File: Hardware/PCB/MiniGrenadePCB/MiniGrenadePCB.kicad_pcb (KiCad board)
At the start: 2 copper layers, 44.5 x 52.1 mm, 3 parts, among them U1 DF-Player_mini, U2 WeMos_D1_mini

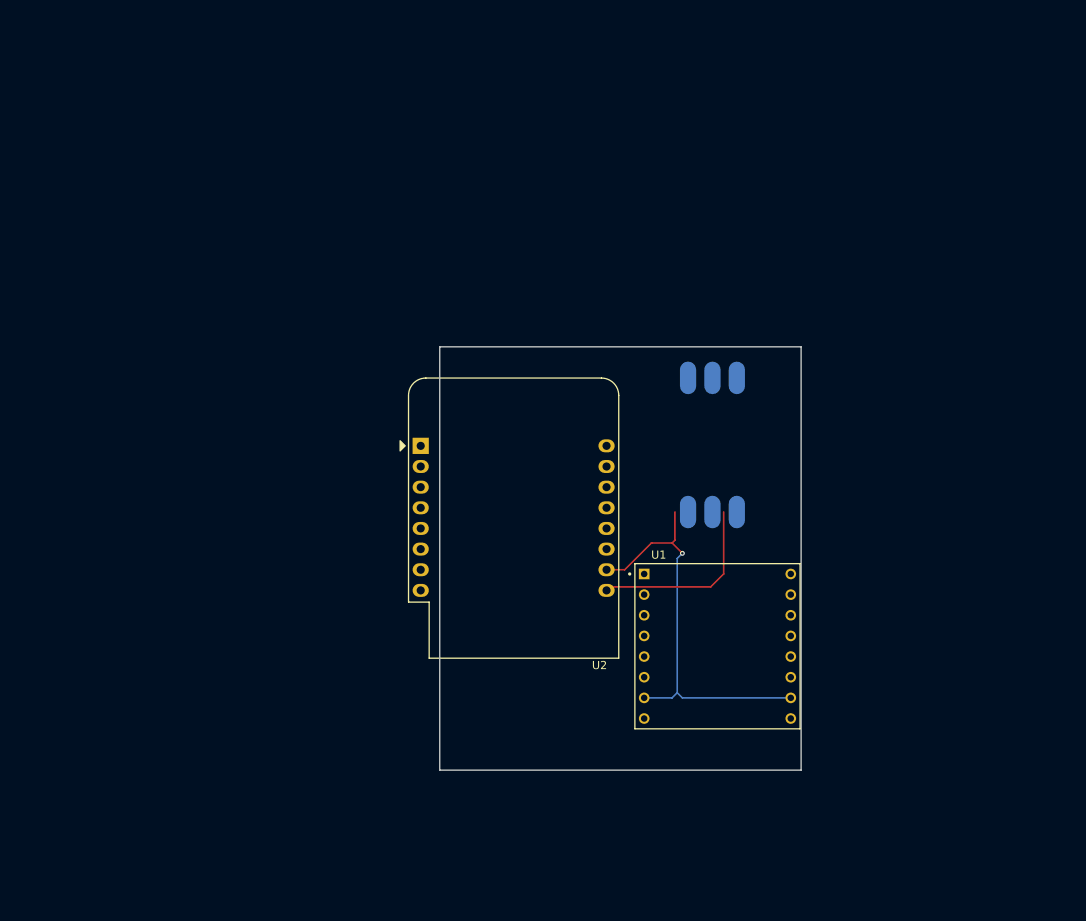
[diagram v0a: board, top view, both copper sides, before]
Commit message: Started working on the bayonet for the mini grenade
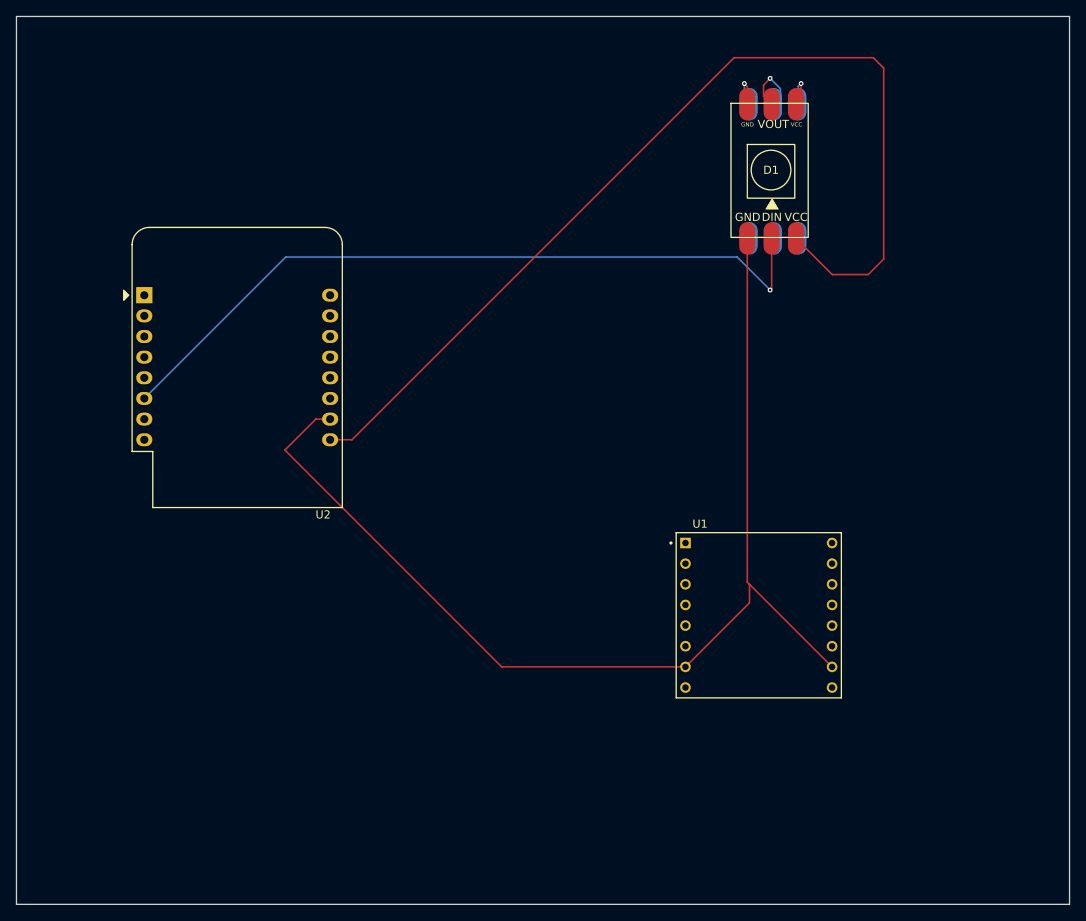
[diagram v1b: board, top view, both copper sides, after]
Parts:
- added D2: WS2812B Neopixel, Grenade_Stuff:NeoPixel_strip, B.Cu at (227.3, 47.0)
- D1: moved to F.Cu
- moved U2 38.7 mm to (149.1, 61.6)
- moved D1 34.8 mm to (227.1, 45.7), turned to 0 degrees
- moved U1 6.35 mm to (224.7, 101.0)
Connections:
- D1 pad 1: unconnected-(D1-DIN-Pad1) -> Net-(U2-GND)
- D1 pad 2: Net-(D1-VCC) -> Net-(D1-DIN)
- D1 pad 3: unconnected-(D1-GND1-Pad3) -> Net-(U2-5V)
- D1 pad 4: unconnected-(D1-DOUT-Pad4) -> Net-(D1-GND-Pad4)
- D1 pad 5: unconnected-(D1-VCC1-Pad5) -> Net-(D1-DOUT)
- U1 pad 10: Net-(D1-GND) -> Net-(U2-GND)
- U1 pad 7: Net-(D1-GND) -> Net-(U2-GND)
- U2 pad 10: Net-(D1-GND) -> Net-(U2-GND)
- U2 pad 6: unconnected-(U2-MOSI/D7-Pad6) -> Net-(D1-DIN)
- U2 pad 9: Net-(D1-VCC) -> Net-(U2-5V)
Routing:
- net Net-(U2-GND): track 0.00 -> 137.9 mm
- net Net-(U2-5V): track 0.00 -> 125.0 mm
- net Net-(D1-DIN): track 0.00 -> 92.3 mm, vias 0 -> 1
- net Net-(D1-GND): track 51.1 -> 0.00 mm, vias 1 -> 0
- net Net-(D1-VCC): track 22.9 -> 0.00 mm
- net Net-(D1-DOUT): track 0.00 -> 8.27 mm, vias 0 -> 1
- net Net-(D1-GND-Pad4): track 0.00 -> 5.50 mm, vias 0 -> 1
- net Net-(D1-VCC-Pad6): track 0.00 -> 5.49 mm, vias 0 -> 1
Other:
- board size 44.5 x 52.1 mm -> 129.5 x 109.2 mm
